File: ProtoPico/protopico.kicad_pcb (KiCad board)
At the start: 2 copper layers, 86.4 x 86.4 mm, 36 parts, among them J1 Screw_Terminal_01x02, J2 Backpack, J3 Other Fin, J4 BoopSensor, J5 Badger, J6 Face Power, J7 Face Matrices, M1 Fan, U1 Pimoroni_TinyRP2040, U2 Pololu D36V28F5, U3 Pololu D24V10F3, U4 74LS125

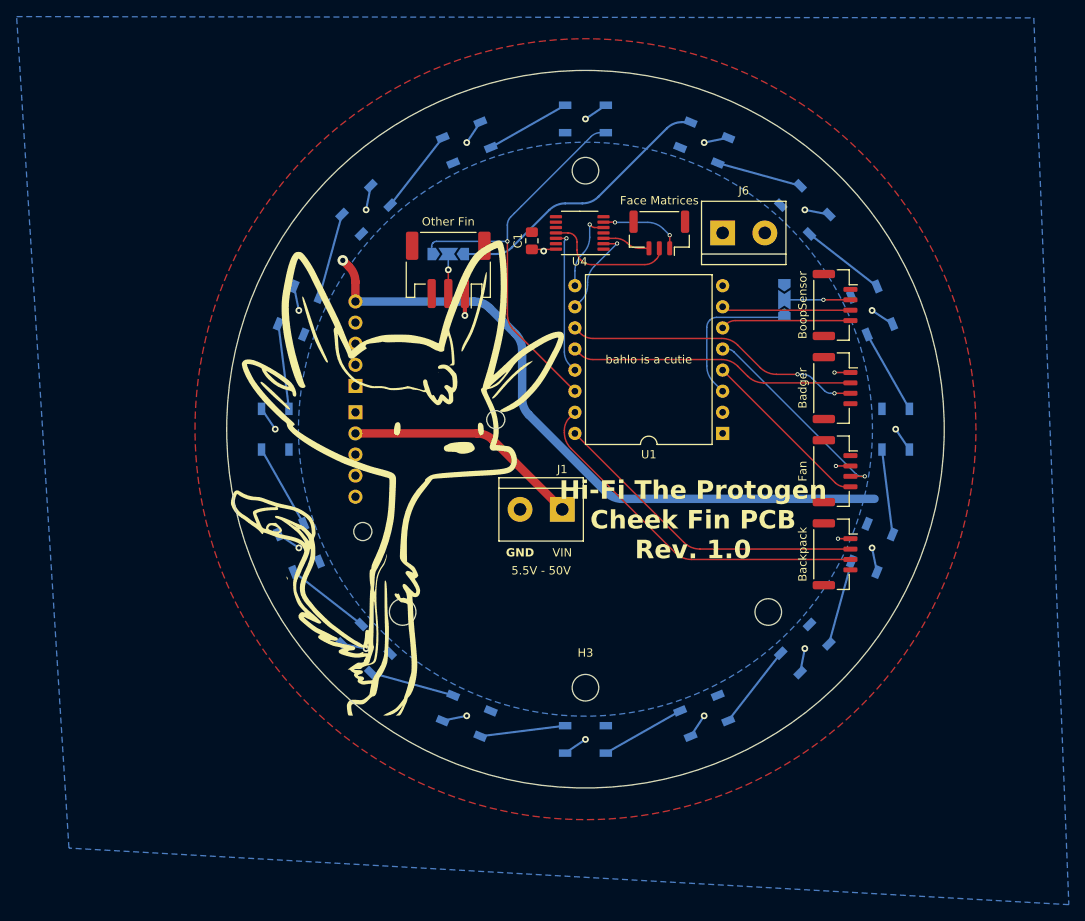
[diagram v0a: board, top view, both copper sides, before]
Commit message: Update cheek pcb to Rev 2
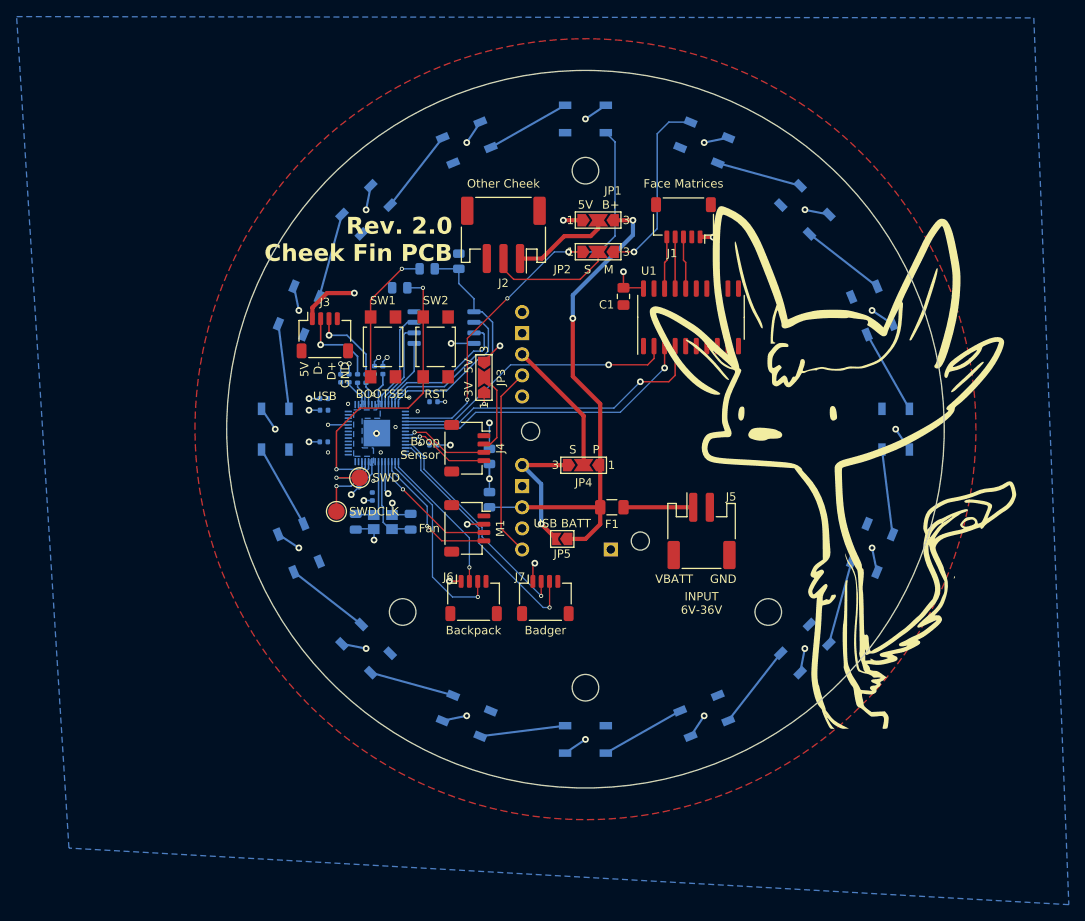
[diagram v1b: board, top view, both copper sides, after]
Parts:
- removed the J6 at (166.4, 76.2)
- removed the J7 at (158.8, 76.2)
- removed U4: 74LS125, Package_SO:TSSOP-14_4.4x5mm_P0.65mm
- added C10: 100n, Capacitor_SMD:C_0402_1005Metric, B.Cu at (118.4, 101.3)
- added C11: 100n, Capacitor_SMD:C_0402_1005Metric, B.Cu at (124.2, 107.9)
- added C12: 100n, Capacitor_SMD:C_0402_1005Metric, B.Cu at (122.9, 106.4)
- added C13: 15pF, Capacitor_SMD:C_0805_2012Metric, B.Cu at (128.8, 111.0)
- added C14: 15pF, Capacitor_SMD:C_0805_2012Metric, B.Cu at (122.2, 111.0)
- added C2: 1uF, Capacitor_SMD:C_0402_1005Metric, B.Cu at (125.5, 92.7)
- added C3: 1uF, Capacitor_SMD:C_0402_1005Metric, B.Cu at (124.5, 92.7)
- added C4: 100n, Capacitor_SMD:C_0402_1005Metric, B.Cu at (121.4, 93.7)
- added C5: 100n, Capacitor_SMD:C_0402_1005Metric, B.Cu at (120.4, 93.7)
- added C6: 100n, Capacitor_SMD:C_0402_1005Metric, B.Cu at (131.6, 96.5)
- added C7: 100n, Capacitor_SMD:C_0402_1005Metric, B.Cu at (118.4, 96.1)
- added C8: 100n, Capacitor_SMD:C_0402_1005Metric, B.Cu at (118.4, 97.5)
- added C9: 100n, Capacitor_SMD:C_0402_1005Metric, B.Cu at (131.6, 101.7)
- added F1: 1A, Fuse:Fuse_1206_3216Metric, F.Cu at (153.0, 109.2)
- added J2: Other Fin, Connector_JST:JST_PH_S3B-PH-SM4-TB_1x03-1MP_P2.00mm_Horizontal, F.Cu at (140.0, 76.4)
- added J5: S2B-PH-SM4-TB, Connector_JST:JST_PH_S2B-PH-SM4-TB_1x02-1MP_P2.00mm_Horizontal, F.Cu at (163.8, 112.1)
- added JP1: SolderJumper_3_Open, Jumper:SolderJumper-3_P2.0mm_Open_TrianglePad1.0x1.5mm_NumberLabels, F.Cu at (151.4, 74.7)
- added JP4: SolderJumper_3_Open, Jumper:SolderJumper-3_P2.0mm_Open_TrianglePad1.0x1.5mm_NumberLabels, F.Cu at (149.6, 104.1)
- added JP5: 5V Jumper, Jumper:SolderJumper-2_P1.3mm_Open_TrianglePad1.0x1.5mm, F.Cu at (147.1, 113.0)
- added R1: 10k, Resistor_SMD:R_0805_2012Metric, B.Cu at (134.6, 79.6)
- added R2: 1k, Resistor_SMD:R_0805_2012Metric, B.Cu at (130.8, 80.5)
- added R3: 10k, Resistor_SMD:R_0805_2012Metric, B.Cu at (127.5, 82.8)
- added R4: 27Ω, Resistor_SMD:R_0402_1005Metric, B.Cu at (123.4, 93.7)
- added R5: 27Ω, Resistor_SMD:R_0402_1005Metric, B.Cu at (122.4, 93.7)
- added R6: 10k, Resistor_SMD:R_0805_2012Metric, B.Cu at (138.3, 103.1)
- added R7: 56k, Resistor_SMD:R_0805_2012Metric, B.Cu at (138.3, 108.3)
- added SW1: TL3305AF160QG, Button_Switch_SMD:SW_SPST_TL3305A, F.Cu at (125.5, 89.9)
- added SW2: TL3305AF160QG, Button_Switch_SMD:SW_SPST_TL3305A, F.Cu at (131.8, 89.9)
- added TP1: TestPoint, TestPoint:TestPoint_Pad_D2.0mm, F.Cu at (122.7, 105.7)
- added TP2: TestPoint, TestPoint:TestPoint_Pad_D2.0mm, F.Cu at (119.9, 109.7)
- added U3: RP2040, Package_DFN_QFN:QFN-56-1EP_7x7mm_P0.4mm_EP3.2x3.2mm, B.Cu at (124.8, 100.3)
- added VR2: Pololu D24V22F5, ProtoPico_Footprints:D24V22FX, B.Cu at (141.0, 115.6)
- added Y1: 12MHz 3225 SMD, Crystal:Crystal_SMD_3225-4Pin_3.2x2.5mm, B.Cu at (125.5, 111.0)
- C1: value C_Small -> 100n
- D1, D10, D11, D12, D13, D14, D15, D16, D2, D3, D4, D5, D6, D7, D8, D9: value SK6812RGBW -> SKC6812RGBW-NW-B
- J1: value Screw_Terminal_01x02 -> Face Matrices; footprint TerminalBlock:TerminalBlock_bornier-2_P5.08mm -> ProtoPico_Footprints:JST_SH_SM05B-SRSS-TB_1x05-1MP_P1.00mm_Horizontal
- J3: value Other Fin -> SM04B-SRSS-TB; footprint Connector_JST:JST_PH_S3B-PH-SM4-TB_1x03-1MP_P2.00mm_Horizontal -> ProtoPico_Footprints:JST_SH_SM04B-SRSS-TB_1x04-1MP_P1.00mm_Horizontal
- J4, M1: footprint Connector_JST:JST_GH_SM04B-GHS-TB_1x04-1MP_P1.25mm_Horizontal -> ProtoPico_Footprints:JST_SH_SM04B-SRSS-TB_1x04-1MP_P1.00mm_Horizontal
- J6: renamed from J2; footprint Connector_JST:JST_GH_SM04B-GHS-TB_1x04-1MP_P1.25mm_Horizontal -> ProtoPico_Footprints:JST_SH_SM04B-SRSS-TB_1x04-1MP_P1.00mm_Horizontal
- J7: renamed from J5; footprint Connector_JST:JST_GH_SM04B-GHS-TB_1x04-1MP_P1.25mm_Horizontal -> ProtoPico_Footprints:JST_SH_SM04B-SRSS-TB_1x04-1MP_P1.00mm_Horizontal
- JP2: moved to F.Cu
- JP3: renamed from JP1; moved to F.Cu
- U1: value Pimoroni_TinyRP2040 -> SN74LS541NSR; footprint MCU_RaspberryPi_and_Boards:Pimoroni_TinyRP2040 -> Package_SO:SO-20_5.3x12.6mm_P1.27mm
- U2: value Pololu D36V28F5 -> W25Q64JVSSIQ; footprint MyloLibrary:Pololu D36V28Fx -> Package_SO:SOIC-8_5.23x5.23mm_P1.27mm
- VR1: renamed from U3; footprint MyloLibrary:Pololu D24V10Fx -> ProtoPico_Footprints:D24V10Fx
- moved G*** 49.0 mm to (176.3, 104.1)
- moved J4 47.5 mm to (135.6, 102.1)
- moved M1 44.8 mm to (135.6, 111.8)
- moved J6 43.8 mm to (136.4, 120.1), turned to 0 degrees
- moved J7 43.1 mm to (145.0, 120.1), turned to 0 degrees
- moved J1 37.7 mm to (161.7, 74.7)
- moved JP3 37.3 mm to (137.7, 93.6)
- moved U2 23.0 mm to (132.8, 87.6), turned to 180 degrees
- moved VR1 19.0 mm to (141.0, 97.2), turned to 90 degrees
- moved JP2 18.0 mm to (151.4, 78.5), turned to 0 degrees
- moved J3 16.8 mm to (118.5, 88.5), turned to 0 degrees
- moved U1 14.5 mm to (162.6, 86.4), turned to 90 degrees
- moved C1 12.9 mm to (154.4, 83.8), turned to -90 degrees
- renumbered H4 to H3, H3 to H4
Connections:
- C1 pad 1: VBUS -> +5V
- D1 pad 1: VDD -> +3.3V
- D10 pad 1: VDD -> +3.3V
- D11 pad 1: VDD -> +3.3V
- D12 pad 1: VDD -> +3.3V
- D13 pad 1: VDD -> +3.3V
- D14 pad 1: VDD -> +3.3V
- D15 pad 1: VDD -> +3.3V
- D16 pad 1: VDD -> +3.3V
- D2 pad 1: VDD -> +3.3V
- D3 pad 1: VDD -> +3.3V
- D4 pad 1: VDD -> +3.3V
- D5 pad 1: VDD -> +3.3V
- D6 pad 1: VDD -> +3.3V
- D7 pad 1: VDD -> +3.3V
- D8 pad 1: VDD -> +3.3V
- D9 pad 1: VDD -> +3.3V
- J1 pad 1: Net-(J1-Pin_1) -> +5V
- J3 pad 1: VBUS -> +5V
- J3 pad 2: /Fin_IO -> D-
- J3 pad 3: GND -> D+
- J6 pad 1: VBUS -> +5V
- J7 pad 1: VBUS -> +5V
- JP2 pad 1: Ring DOUT -> Ring DIN
- JP2 pad 3: Ring DIN -> Ring DOUT
- JP3 pad 1: +3V3 -> +3.3V
- JP3 pad 3: VBUS -> +5V
- M1 pad 2: VBUS -> +5V
- U1 pad 1: VBUS -> GND
- U1 pad 10: Face SCK_3.3 -> GND
- U1 pad 11: UART1 RX -> unconnected-(U1-Y7-Pad11)
- U1 pad 12: UART1 TX -> unconnected-(U1-Y6-Pad12)
- U1 pad 13: Face CS_3.3 -> unconnected-(U1-Y5-Pad13)
- U1 pad 14: Ring DIN -> unconnected-(U1-Y4-Pad14)
- U1 pad 15: UART0 RX -> unconnected-(U1-Y3-Pad15)
- U1 pad 16: UART0 TX -> Face TX
- U1 pad 2: GND -> Face SCK_3.3
- U1 pad 3: +3V3 -> Face CS_3.3
- U1 pad 4: Fan Tach -> Face TX_3.3
- U1 pad 5: Fan PWM -> GND
- U1 pad 6: SCL1 -> GND
- U1 pad 7: SDA1 -> GND
- U1 pad 9: Face TX_3.3 -> GND
- U2 pad 1: unconnected-(U2-EN-Pad1) -> /Microcontroller/SIO_~{CS}
- U2 pad 2: Net-(J1-Pin_1) -> /Microcontroller/SIO1
- U2 pad 3: GND -> /Microcontroller/SIO2
- U2 pad 5: VBUS -> /Microcontroller/SIO0
- VR1 pad 2: unconnected-(U3-~{SHDN}-Pad2) -> 5V_PG
- VR1 pad 3: VBUS -> /3V3_IN
- VR1 pad 5: VDD -> +3.3V
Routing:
- net VDD: track 82.0 -> 0.00 mm, vias 1 -> 0
- net +BATT: track 0.00 -> 61.1 mm, vias 0 -> 2
- net +5V: track 0.00 -> 39.5 mm, vias 0 -> 9
- net RUN: track 0.00 -> 35.3 mm, vias 0 -> 2
- net GND: track 47.3 -> 77.4 mm, vias 16 -> 33
- net VSENSE: track 0.00 -> 29.7 mm, vias 0 -> 2
- net /Microcontroller/SIO_~{CS}: track 0.00 -> 29.5 mm
- net Face TX_3.3: track 9.62 -> 38.5 mm
- net Net-(J1-Pin_1): track 28.5 -> 0.00 mm
- net Face SCK_3.3: track 11.1 -> 34.6 mm
- net 5V_PG: track 0.00 -> 23.1 mm
- net UART0 TX: track 38.8 -> 17.9 mm, vias 0 -> 1
- net UART0 RX: track 44.0 -> 24.1 mm, vias 0 -> 1
- net Face CS_3.3: track 17.6 -> 36.8 mm
- net /Microcontroller/SIO1: track 0.00 -> 19.0 mm
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- added copper zone on B.Cu, net +1V1
- added copper zone on B.Cu, net +3.3V
- added copper zone on In1.Cu, net +3.3V
- added copper zone on In1.Cu, net +5V
- added copper zone on In2.Cu, net GND
- removed copper zone on B.Cu, net VBUS
- removed copper zone on B.Cu, net VDD
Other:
- copper layers 2 -> 4
- board text added: "3V"
- board text added: "5V D- D+ GND"
- board text added: "B+"
- board text added: "BOOTSEL"
- board text added: "Backpack"
- board text added: "Badger"
- board text added: "Boop Sensor"
- board text added: "Face Matrices"
- board text added: "Fan"
- board text added: "INPUT 6V-36V"
- board text added: "M"
- board text added: "Other Cheek"
- board text added: "P"
- board text added: "RST"
- board text added: "Rev. 2.0 Cheek Fin PCB"
- board text added: "S"
- board text added: "SWD"
- board text added: "SWDCLK"
- board text added: "USB"
- board text added: "USB BATT"
- board text added: "VBATT"
- board text removed: "1"
- board text removed: "3"
- board text removed: "3.3V"
- board text removed: "5.5V - 50V"
- board text removed: "Hi-Fi The Protogen Cheek Fin PCB Rev. 1.0"
- board text removed: "JP1 JP2"
- board text removed: "MAIN"
- board text removed: "SUB"
- board text removed: "VIN"
- board text removed: "bahlo is a cutie"

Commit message: Update to V2 of Backpack
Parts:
- removed the G*** at (176.3, 104.1)
- removed the H2 at (127.9, 121.8)
- removed H3: MountingHole, MountingHole:MountingHole_3.2mm_M3
- removed the J6 at (136.4, 120.1)
- removed the J7 at (145.0, 120.1)
- removed JP2, JP3, JP4: SolderJumper_3_Open, Jumper:SolderJumper-3_P2.0mm_Open_TrianglePad1.0x1.5mm_NumberLabels
- removed JP5: 5V Jumper, Jumper:SolderJumper-2_P1.3mm_Open_TrianglePad1.0x1.5mm
- removed the R1 at (134.6, 79.6)
- removed TP1, TP2: TestPoint, TestPoint:TestPoint_Pad_D2.0mm
- added C15: 10uF, Capacitor_SMD:C_0805_2012Metric, B.Cu at (168.8, 99.6)
- added C16: 100nF, Capacitor_SMD:C_0603_1608Metric, B.Cu at (168.7, 101.3)
- added C17: 22uF, Capacitor_SMD:C_0805_2012Metric, B.Cu at (167.5, 107.4)
- added C18: 22uF, Capacitor_SMD:C_0805_2012Metric, B.Cu at (165.5, 107.4)
- added C19: 100nF, Capacitor_SMD:C_0603_1608Metric, B.Cu at (163.7, 107.2)
- added C20: 10uF, Capacitor_SMD:C_0805_2012Metric, B.Cu at (175.4, 101.3)
- added C21: 100nF, Capacitor_SMD:C_0603_1608Metric, B.Cu at (175.5, 99.6)
- added C22: 22uF, Capacitor_SMD:C_0805_2012Metric, B.Cu at (176.6, 93.4)
- added C23: 22uF, Capacitor_SMD:C_0805_2012Metric, B.Cu at (178.7, 93.4)
- added C24: 100nF, Capacitor_SMD:C_0603_1608Metric, B.Cu at (180.5, 93.5)
- added D17: BAT201M3 RRG, Diode_SMD:D_SOD-323_HandSoldering, F.Cu at (157.1, 102.2)
- added G***: LOGO, LOGO, F.Cu at (141.4, 114.9)
- added G***: LOGO, LOGO, B.Cu at (132.5, 107.2)
- added G***: LOGO, LOGO, B.Cu at (165.7, 100.5)
- added J8: JST-SH, Connector_JST:JST_SH_SM03B-SRSS-TB_1x03-1MP_P1.00mm_Horizontal, F.Cu at (113.3, 102.9)
- added J9: GPIO, Connector_JST:JST_GH_SM06B-GHS-TB_1x06-1MP_P1.25mm_Horizontal, F.Cu at (147.5, 101.0)
- added L1: SRN6045-3R3Y, Inductor_SMD:L_Bourns-SRN6028, B.Cu at (172.3, 106.2)
- added L2: SRN6045-4R7Y, Inductor_SMD:L_Bourns-SRN6028, B.Cu at (171.7, 94.7)
- added R10: 30k, Resistor_SMD:R_0805_2012Metric_Pad1.20x1.40mm_HandSolder, F.Cu at (172.3, 107.7)
- added R11: 10k, Resistor_SMD:R_0402_1005Metric, B.Cu at (164.2, 102.6)
- added R13: 220k, Resistor_SMD:R_0402_1005Metric, B.Cu at (181.5, 98.3)
- added R15: 30k, Resistor_SMD:R_0402_1005Metric, B.Cu at (180.0, 98.8)
- added R16: 100, Resistor_SMD:R_0402_1005Metric, B.Cu at (118.8, 106.8)
- added R17: 100, Resistor_SMD:R_0402_1005Metric, B.Cu at (118.8, 105.8)
- added R3: 100, Resistor_SMD:R_0402_1005Metric, B.Cu at (155.4, 73.9)
- added R8: 182k, Resistor_SMD:R_0805_2012Metric_Pad1.20x1.40mm_HandSolder, F.Cu at (172.3, 105.7)
- added R9: 45.3k, Resistor_SMD:R_0402_1005Metric, B.Cu at (162.7, 103.1)
- C1: footprint Capacitor_SMD:C_0805_2012Metric_Pad1.18x1.45mm_HandSolder -> Capacitor_SMD:C_0402_1005Metric; moved to B.Cu
- C13, C14: footprint Capacitor_SMD:C_0805_2012Metric -> Capacitor_SMD:C_0402_1005Metric
- F1: footprint Fuse:Fuse_1206_3216Metric -> Fuse:Fuse_1206_3216Metric_Pad1.42x1.75mm_HandSolder
- H1: value MountingHole -> M3 Hole; footprint MountingHole:MountingHole_3.2mm_M3 -> MountingHole:MountingHole_3.2mm_M3_ISO14580; moved to B.Cu
- H2: renamed from H4; value MountingHole -> M3 Hole; footprint MountingHole:MountingHole_3.2mm_M3 -> MountingHole:MountingHole_3.2mm_M3_ISO14580; moved to B.Cu
- J2: renamed from J4; footprint ProtoPico_Footprints:JST_SH_SM04B-SRSS-TB_1x04-1MP_P1.00mm_Horizontal -> Connector_JST:JST_GH_SM04B-GHS-TB_1x04-1MP_P1.25mm_Horizontal
- J4: renamed from J1; value Face Matrices -> S5B-PH-SM4-TB; footprint ProtoPico_Footprints:JST_SH_SM05B-SRSS-TB_1x05-1MP_P1.00mm_Horizontal -> Connector_JST:JST_PH_S5B-PH-SM4-TB_1x05-1MP_P2.00mm_Horizontal
- J6: renamed from J2; value Other Fin -> S3B-PH-SM4-TB
- J7: renamed from J3; footprint ProtoPico_Footprints:JST_SH_SM04B-SRSS-TB_1x04-1MP_P1.00mm_Horizontal -> Connector_JST:JST_PH_S4B-PH-SM4-TB_1x04-1MP_P2.00mm_Horizontal
- JP1: value SolderJumper_3_Open -> Voltage Select; footprint Jumper:SolderJumper-3_P2.0mm_Open_TrianglePad1.0x1.5mm_NumberLabels -> Jumper:SolderJumper-3_P1.3mm_Open_RoundedPad1.0x1.5mm
- M1: footprint ProtoPico_Footprints:JST_SH_SM04B-SRSS-TB_1x04-1MP_P1.00mm_Horizontal -> Connector_JST:JST_GH_SM04B-GHS-TB_1x04-1MP_P1.25mm_Horizontal
- R1: renamed from R7; footprint Resistor_SMD:R_0805_2012Metric -> Resistor_SMD:R_0805_2012Metric_Pad1.20x1.40mm_HandSolder; moved to F.Cu
- R2: renamed from R6; value 10k -> 12k; footprint Resistor_SMD:R_0805_2012Metric -> Resistor_SMD:R_0805_2012Metric_Pad1.20x1.40mm_HandSolder; moved to F.Cu
- R7: renamed from R3; footprint Resistor_SMD:R_0805_2012Metric -> Resistor_SMD:R_0402_1005Metric
- U1: footprint Package_SO:SO-20_5.3x12.6mm_P1.27mm -> Package_SO:TSSOP-20_4.4x6.5mm_P0.65mm; moved to B.Cu
- VR1: value Pololu D24V10F3 -> TPS564255; footprint ProtoPico_Footprints:D24V10Fx -> Package_TO_SOT_SMD:SOT-563
- VR2: value Pololu D24V22F5 -> TPS564255; footprint ProtoPico_Footprints:D24V22FX -> Package_TO_SOT_SMD:SOT-563
- moved VR2 40.5 mm to (177.1, 97.3), turned to 0 degrees
- moved VR1 26.9 mm to (167.1, 103.6), turned to 180 degrees
- moved SW1 25.7 mm to (150.3, 83.2)
- moved R7 23.5 mm to (118.2, 104.4)
- moved JP1 22.6 mm to (145.7, 96.5), turned to 180 degrees
- moved R2 20.7 mm to (154.7, 115.8), turned to -90 degrees
- moved R1 16.6 mm to (154.7, 111.2), turned to -90 degrees
- moved SW2 14.8 mm to (145.0, 83.2)
- moved R4 14.4 mm to (140.3, 91.3), turned to 0 degrees
- moved C1 14.3 mm to (168.4, 81.0)
- moved J2 12.8 mm to (127.0, 111.5), turned to 0 degrees
- moved M1 10.8 mm to (136.5, 101.0), turned to 0 degrees
- moved J4 10.1 mm to (165.4, 84.1)
- moved J6 8.10 mm to (136.1, 83.6)
- moved J7 7.19 mm to (123.7, 83.6)
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- renumbered C6 to C10, C9 to C11, C3 to C12, C12 to C2, C4 to C3, C2 to C4, C11 to C5, C5 to C6, C10 to C7, C7 to C9, R2 to R4, R4 to R5, R5 to R6
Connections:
- D16 pad 2: Ring DOUT -> Net-(D16-DOUT)
- J2 pad 2: /BoopVCC -> +3.3V
- J6 pad 1: Net-(J2-Pin_1) -> +5V
- J6 pad 2: /Fin_IO -> Ring DOUT
- J7 pad 1: +5V -> /Microcontroller/VUSB
- JP1 pad 1: +5V -> +3.3V
- JP1 pad 2: Net-(J2-Pin_1) -> Net-(J9-Pin_2)
- JP1 pad 3: +BATT -> +5V
- U1 pad 16: Face TX -> Face SCK
- U1 pad 18: Face SCK -> Face TX
- U1 pad 2: Face SCK_3.3 -> Face TX_3.3
- U1 pad 4: Face TX_3.3 -> Face SCK_3.3
- U3 pad 11: UART1 TX -> /Microcontroller/GPIO8
- U3 pad 12: UART1 RX -> /Microcontroller/GPIO9
- U3 pad 13: unconnected-(U3-GPIO10-Pad13) -> /Microcontroller/GPIO10
- U3 pad 14: unconnected-(U3-GPIO11-Pad14) -> /Microcontroller/GPIO11
- U3 pad 15: UART0 TX -> Fan PWM
- U3 pad 16: UART0 RX -> Fan Tach
- U3 pad 17: Fan Tach -> 5V_EN
- U3 pad 18: Fan PWM -> 5V_PG
- VR1 pad 1: unconnected-(VR1-PG-Pad1) -> +BATT
- VR1 pad 2: 5V_PG -> Net-(VR1-SW)
- VR1 pad 3: /3V3_IN -> GND
- VR1 pad 4: GND -> unconnected-(VR1-PG-Pad4)
- VR1 pad 5: +3.3V -> /Voltage Regulators/3V3_EN
- VR2 pad 1: 5V_PG -> +BATT
- VR2 pad 2: unconnected-(VR2-EN-Pad2) -> Net-(VR2-SW)
- VR2 pad 3: +BATT -> GND
- VR2 pad 4: GND -> 5V_PG
- VR2 pad 5: +5V -> 5V_EN
- VR2 pad 6: GND -> /Voltage Regulators/5V_FB
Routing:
- net 5V_EN: track 0.00 -> 60.9 mm, vias 0 -> 2
- net /Microcontroller/VUSB: track 0.00 -> 46.1 mm, vias 0 -> 2
- net 5V_PG: track 23.1 -> 63.1 mm, vias 0 -> 2
- net +BATT: track 61.1 -> 29.5 mm, vias 2 -> 5
- net UART1 RX: track 30.4 -> 0.00 mm, vias 1 -> 0
- net +3.3V: track 1.17 -> 31.0 mm, vias 10 -> 12
- net UART1 TX: track 27.2 -> 0.00 mm, vias 1 -> 0
- net /Microcontroller/GPIO11: track 0.00 -> 25.4 mm, vias 0 -> 1
- net /Microcontroller/GPIO10: track 0.00 -> 24.1 mm, vias 0 -> 1
- net UART0 RX: track 24.1 -> 0.00 mm, vias 1 -> 0
- net /Microcontroller/GPIO9: track 0.00 -> 22.8 mm, vias 0 -> 1
- net /Microcontroller/GPIO8: track 0.00 -> 21.5 mm, vias 0 -> 1
- net UART0 TX: track 17.9 -> 0.00 mm, vias 1 -> 0
- net VSENSE: track 29.7 -> 46.2 mm
- net /3V3_IN: track 16.4 -> 0.00 mm
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- added copper zone on B.Cu, net +5V
- added copper zone on In2.Cu, net +5V
- added copper zone on B.Cu, net +BATT
- added copper zone on F.Cu, net +BATT
- added copper zone on B.Cu, net GND
- added copper zone on B.Cu, net Net-(VR1-SW)
- added copper zone on B.Cu, net Net-(VR2-SW)
- removed copper zone on In1.Cu, net +5V
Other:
- board text added: "+3.3V"
- board text added: "+5V"
- board text added: "6V-17V DC 1A FUSE"
- board text added: "BOOP"
- board text added: "BOOT"
- board text added: "CHEEK"
- board text added: "CLK"
- board text added: "CS"
- board text added: "D+"
- board text added: "D-"
- board text added: "DIN"
- board text added: "DOUT"
- board text added: "Design by @MyloWhylo"
- board text added: "FAN"
- board text added: "GPIO10"
- board text added: "GPIO11"
- board text added: "GPIO8"
- board text added: "GPIO9"
- board text added: "KnightRider Edition"
- board text added: "MATRICES"
- board text added: "PWM"
- board text added: "PWR"
- board text added: "ProtoPico v3.0"
- board text added: "SCK"
- board text added: "SCL1"
- board text added: "SDA1"
- board text added: "TACH"
- board text removed: "3V"
- board text removed: "5V"
- board text removed: "5V D- D+ GND"
- board text removed: "B+"
- board text removed: "BOOTSEL"
- board text removed: "Backpack"
- board text removed: "Badger"
- board text removed: "Boop Sensor"
- board text removed: "Face Matrices"
- board text removed: "Fan"
- board text removed: "INPUT 6V-36V"
- board text removed: "M"
- board text removed: "Other Cheek"
- board text removed: "P"
- board text removed: "Rev. 2.0 Cheek Fin PCB"
- board text removed: "S"
- board text removed: "SWDCLK"
- board text removed: "USB BATT"
